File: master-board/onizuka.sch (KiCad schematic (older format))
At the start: 27 parts, among them IC1 FT232RQ, IC2 ADCMP371, P1 USB_OTG, P2 FTDI, P3 EXTRA, Q1 Q_PMOS_DGS, SW1 SWITCH_INV, U1 LD1117S33TR

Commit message: Slight schematic rework, much PCB faffing
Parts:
- removed P2: FTDI, Pin_Headers:Pin_Header_Angled_1x06, symbol CONN_01X06
- removed P3: EXTRA, Pin_Headers:Pin_Header_Angled_1x04, symbol CONN_01X04
- added P2: FTDI, Pin_Headers:Pin_Header_Angled_2x06, symbol CONN_02X06
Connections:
- no-connect marks 13 -> 14
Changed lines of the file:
@@
 L GND #PWR02
 U 1 1 573F0E0D
-P 4950 1450
-F 0 "#PWR02" H 4950 1200 50  0001 C CNN
-F 1 "GND" H 4950 1300 50  0000 C CNN
-F 2 "" H 4950 1450 50  0000 C CNN
-F 3 "" H 4950 1450 50  0000 C CNN
-	1    4950 1450
-	1    0    0    -1
-$EndComp
-Text Label 5400 1650 2    60   ~ 0
+P 4950 1900
+F 0 "#PWR02" H 4950 1650 50  0001 C CNN
+F 1 "GND" H 4950 1750 50  0000 C CNN
+F 2 "" H 4950 1900 50  0000 C CNN
+F 3 "" H 4950 1900 50  0000 C CNN
+	1    4950 1900
+	1    0    0    -1
+$EndComp
+Text Label 5400 2100 2    60   ~ 0
 PWROUT
 Wire Wire Line
@@
 	0    1    1    0
 $EndComp
-NoConn ~ 1400 2250
 $Comp
 L ADCMP371 IC2
@@
 	0    -1   -1   0
 $EndComp
-$Comp
-L CONN_01X06 P2
-U 1 1 573F91A3
-P 5600 1700
-F 0 "P2" H 5600 2050 50  0000 C CNN
-F 1 "FTDI" V 5700 1700 50  0000 C CNN
-F 2 "Pin_Headers:Pin_Header_Angled_1x06" H 5600 1700 50  0001 C CNN
-F 3 "" H 5600 1700 50  0000 C CNN
-	1    5600 1700
-	1    0    0    -1
-$EndComp
-$Comp
-L CONN_01X04 P3
-U 1 1 573F91DD
-P 5600 2300
-F 0 "P3" H 5600 2550 50  0000 C CNN
-F 1 "EXTRA" V 5700 2300 50  0000 C CNN
-F 2 "Pin_Headers:Pin_Header_Angled_1x04" H 5600 2300 50  0001 C CNN
-F 3 "" H 5600 2300 50  0000 C CNN
-	1    5600 2300
-	1    0    0    -1
-$EndComp
-Text Label 5400 1550 2    60   ~ 0
+Text Label 5400 2000 2    60   ~ 0
 CTS
-Text Label 5400 1750 2    60   ~ 0
+Text Label 5400 2200 2    60   ~ 0
 TXD
-Text Label 5400 1850 2    60   ~ 0
+Text Label 5400 2300 2    60   ~ 0
 RXD
-Text Label 5400 1950 2    60   ~ 0
+Text Label 5400 2400 2    60   ~ 0
 RTS
 Wire Wire Line
-	4950 1450 5400 1450
+	4950 1900 5400 1900
 Text Label 4400 1450 0    60   ~ 0
 TXD
@@
 Text Label 4400 2150 0    60   ~ 0
 RI
-Text Label 5400 2150 2    60   ~ 0
+Text Label 5900 1900 0    60   ~ 0
 DTR
-Text Label 5400 2250 2    60   ~ 0
+Text Label 5900 2000 0    60   ~ 0
 DSR
-Text Label 5400 2350 2    60   ~ 0
+Text Label 5900 2100 0    60   ~ 0
 DCD
-Text Label 5400 2450 2    60   ~ 0
+Text Label 5900 2200 0    60   ~ 0
 RI
+$Comp
+L CONN_02X06 P2
+U 1 1 57438536
+P 5650 2150
+F 0 "P2" H 5650 2500 50  0000 C CNN
+F 1 "FTDI" H 5650 1800 50  0000 C CNN
+F 2 "Pin_Headers:Pin_Header_Angled_2x06" H 5650 950 50  0001 C CNN
+F 3 "" H 5650 950 50  0000 C CNN
+	1    5650 2150
+	1    0    0    -1
+$EndComp
+NoConn ~ 5900 2300
+NoConn ~ 5900 2400
+$Comp
+L GND #PWR?
+U 1 1 57439366
+P 1400 2250
+F 0 "#PWR?" H 1400 2000 50  0001 C CNN
+F 1 "GND" H 1400 2100 50  0000 C CNN
+F 2 "" H 1400 2250 50  0000 C CNN
+F 3 "" H 1400 2250 50  0000 C CNN
+	1    1400 2250
+	1    0    0    -1
+$EndComp
 $EndSCHEMATC

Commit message: Various upgrades, also ESP-12E footprint for ESP board
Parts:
- added C7: 100n, Capacitors_SMD:C_0603, symbol C_Small
- added C8: 10u, Capacitors_SMD:C_0603, symbol C_Small
- added R9: 10k, Resistors_SMD:R_0603, symbol R_Small
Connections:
- net labels added: 4v5, LEDCTRL, USBD+, USBD-
- wire segments 23 -> 25
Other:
- moved on the sheet: P1

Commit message: Board reshuffle, new regulator
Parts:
- removed U1: LD1117S33TR, SOT-223, symbol LD1117S33TR
- added C9: 1u, Capacitors_SMD:C_0402, symbol C_Small
- added U1: MIC5353-3.3YMT, Housings_MLF:Thin_MLF_6_1.6mm_0.5mm_pitch, symbol MIC5353-3.3YMT
- C1, C2, C3, C4, C5, C6: footprint Capacitors_SMD:C_0603 -> Capacitors_SMD:C_0402
- C7: value 100n -> 1u; footprint Capacitors_SMD:C_0603 -> Capacitors_SMD:C_0402
- C8: value 10u -> 1u; footprint Capacitors_SMD:C_0603 -> Capacitors_SMD:C_0402
- R1, R2, R3, R4, R5, R6, R7, R8, R9: footprint Resistors_SMD:R_0603 -> Resistors_SMD:R_0402
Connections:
- wire segments 25 -> 29

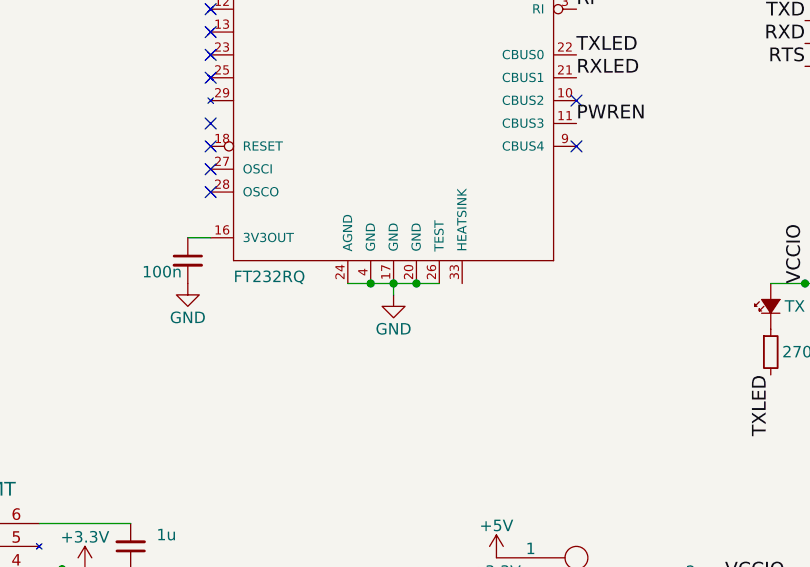
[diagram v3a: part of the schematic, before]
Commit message: Faffing, added connections to heatsink pad on FTDI, moved connector in slightly.
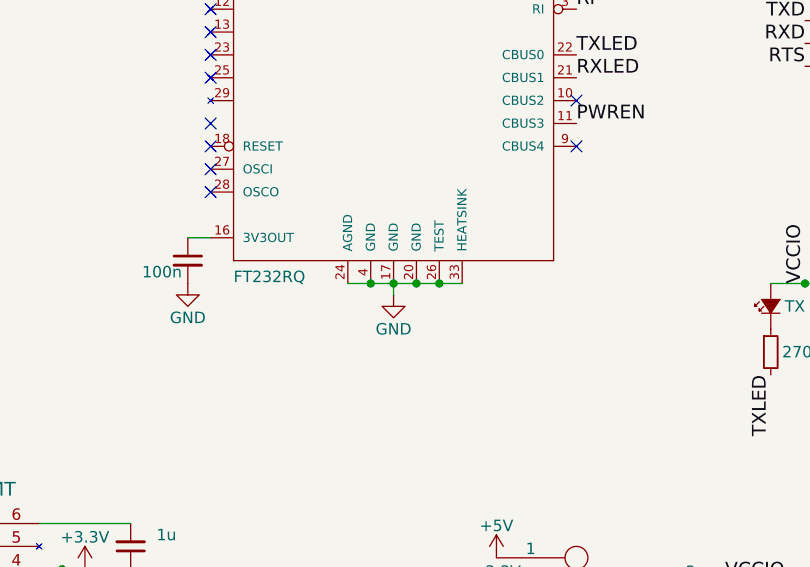
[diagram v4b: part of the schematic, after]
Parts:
- IC1: footprint Housings_DFN_QFN:QFN-32-1EP_5x5mm_Pitch0.5mm -> ftdi4-QFN-32
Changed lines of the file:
@@
 EESchema Schematic File Version 2
+LIBS:onizuka-rescue
 LIBS:power
 LIBS:device
@@
 $EndDescr
 $Comp
-L FT232RQ IC1
-U 1 1 573F0905
-P 3600 2250
-F 0 "IC1" H 2900 3170 50  0000 L BNN
-F 1 "FT232RQ" H 2900 1150 50  0000 L BNN
-F 2 "Housings_DFN_QFN:QFN-32-1EP_5x5mm_Pitch0.5mm" H 3600 2400 50  0001 C CNN
-F 3 "" H 3600 2250 60  0000 C CNN
-	1    3600 2250
-	1    0    0    -1
-$EndComp
-$Comp
 L USB_OTG P1
 U 1 1 573F0976
@@
 $EndComp
 Wire Wire Line
-	3400 3350 3800 3350
+	3400 3350 3900 3350
 Connection ~ 3600 3350
 Connection ~ 3500 3350
@@
 	1    0    0    -1
 $EndComp
+Connection ~ 3800 3350
+$Comp
+L FT232RQ IC1
+U 1 1 574DED0D
+P 3600 2250
+F 0 "IC1" H 2900 3170 50  0000 L BNN
+F 1 "FT232RQ" H 2900 1150 50  0000 L BNN
+F 2 "ftdi4-QFN-32" H 3600 2400 50  0001 C CNN
+F 3 "" H 3600 2250 60  0000 C CNN
+	1    3600 2250
+	1    0    0    -1
+$EndComp

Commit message: Tidied up schema, started to add farnell codes for components.
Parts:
- removed Q1: Q_PMOS_DGS, TO_SOT_Packages_SMD:SOT-23, symbol Q_PMOS_DGS
- added Q1: Q_PMOS_GSD, TO_SOT_Packages_SMD:SOT-23, symbol Q_PMOS_GSD
- IC1: footprint ftdi4-QFN-32 -> Housings_DFN_QFN:QFN-32-1EP_5x5mm_Pitch0.5mm
- IC2: Farnell (none) -> 2376801
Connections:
- net labels added: +4v5
- net labels removed: 4v5
- wire segments 29 -> 34
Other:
- note added: "3v3 Regulator"
- note added: "FTDI"
- note added: "Output Voltage Control"
- note added: "Output power control"
- note added: "Output voltage sense"
- note added: "USB Connector"
- note added: "Voltage Ref"
- moved on the sheet: IC1, P2, U1

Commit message: Various tweaks
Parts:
- removed C2: 10n, Capacitors_SMD:C_0402, symbol CP_Small
- removed C3: 4.7u, Capacitors_SMD:C_0402, symbol CP_Small
- added C2: 10n, Capacitors_SMD:C_0402, symbol C_Small
- added C3: 4u7, Capacitors_SMD:C_0402, symbol C_Small
- IC1: footprint Housings_DFN_QFN:QFN-32-1EP_5x5mm_Pitch0.5mm -> ftdi:FTDI-FT232RQ-QFN-32
- R1, R2, R3: value 270R -> 1k
- R4: value 1k -> 1K
- R5: value 510K -> 51K
- R6: value 4M3 -> 430K
- R7, R8: value 680R -> 1k
- R9: value 10k -> 10K
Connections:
- net +5V: now also C2.1, C3.1
- net GND: now also C2.2, C3.2
- net +4v5: no longer names the net of IC2.3 (-), R5.2, R6.1
- no-connect marks 14 -> 8
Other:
- note removed: "Output voltage sense"
- note removed: "Voltage Ref"

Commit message: Updated switch
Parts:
- removed SW1: SWITCH_INV, Buttons_Switches_ThroughHole:SW_Micro_SPST, symbol SWITCH_INV
- added SW1: SPDT, Wurth:450301014042, symbol SPDT
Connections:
- net +3V3: now also SW1.3
- net +5V: now also SW1.2
- net VCCIO: now also SW1.1
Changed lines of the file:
@@
 LIBS:contrib
 LIBS:valves
-LIBS:ftdi
 LIBS:ad
 LIBS:micrel
-LIBS:power-ext
+LIBS:ftdi
+LIBS:Switches
 LIBS:onizuka-cache
 EELAYER 25 0
@@
 $EndComp
 $Comp
-L SWITCH_INV SW1
-U 1 1 573F1E28
-P 5500 2850
-F 0 "SW1" H 5300 3000 50  0001 C CNN
-F 1 "SWITCH_INV" H 5350 2700 50  0001 C CNN
-F 2 "Buttons_Switches_ThroughHole:SW_Micro_SPST" H 5500 2850 50  0001 C CNN
-F 3 "" H 5500 2850 50  0000 C CNN
-	1    5500 2850
-	-1   0    0    -1
-$EndComp
-$Comp
 L +5V #PWR010
 U 1 1 573F1E7D
-P 5000 2750
-F 0 "#PWR010" H 5000 2600 50  0001 C CNN
-F 1 "+5V" H 5000 2890 50  0000 C CNN
-F 2 "" H 5000 2750 50  0000 C CNN
-F 3 "" H 5000 2750 50  0000 C CNN
-	1    5000 2750
+P 5150 2750
+F 0 "#PWR010" H 5150 2600 50  0001 C CNN
+F 1 "+5V" H 5150 2890 50  0000 C CNN
+F 2 "" H 5150 2750 50  0000 C CNN
+F 3 "" H 5150 2750 50  0000 C CNN
+	1    5150 2750
 	-1   0    0    -1
 $EndComp
@@
 L +3.3V #PWR011
 U 1 1 573F1E91
-P 5000 2950
-F 0 "#PWR011" H 5000 2800 50  0001 C CNN
-F 1 "+3.3V" H 5000 3090 50  0000 C CNN
-F 2 "" H 5000 2950 50  0000 C CNN
-F 3 "" H 5000 2950 50  0000 C CNN
-	1    5000 2950
+P 5150 2950
+F 0 "#PWR011" H 5150 2800 50  0001 C CNN
+F 1 "+3.3V" H 5150 3090 50  0000 C CNN
+F 2 "" H 5150 2950 50  0000 C CNN
+F 3 "" H 5150 2950 50  0000 C CNN
+	1    5150 2950
 	-1   0    0    -1
 $EndComp
-Text Label 6000 2850 0    60   ~ 0
+Text Label 5950 2850 0    60   ~ 0
 VCCIO
 Text Label 2900 3250 2    60   ~ 0
@@
 L PWR_FLAG #FLG013
 U 1 1 573F27A3
-P 6000 2850
-F 0 "#FLG013" H 6000 2945 50  0001 C CNN
-F 1 "PWR_FLAG" H 6000 3030 50  0000 C CNN
-F 2 "" H 6000 2850 50  0000 C CNN
-F 3 "" H 6000 2850 50  0000 C CNN
-	1    6000 2850
+P 5950 2850
+F 0 "#FLG013" H 5950 2945 50  0001 C CNN
+F 1 "PWR_FLAG" H 5950 3030 50  0000 C CNN
+F 2 "" H 5950 2850 50  0000 C CNN
+F 3 "" H 5950 2850 50  0000 C CNN
+	1    5950 2850
 	-1   0    0    1
 $EndComp
@@
 	1    0    0    -1
 $EndComp
-Connection ~ 6000 2850
+Connection ~ 5950 2850
 $Comp
 L FT232RQ IC1
@@
 	1    0    0    -1
 $EndComp
+$Comp
+L SPDT SW1
+U 1 1 574EF3CB
+P 5550 2850
+F 0 "SW1" H 5550 2500 60  0001 C CNN
+F 1 "SPDT" H 5550 3150 60  0001 C CNN
+F 2 "Wurth:450301014042" H 5600 2850 60  0001 C CNN
+F 3 "" H 5600 2850 60  0000 C CNN
+	1    5550 2850
+	1    0    0    -1
+$EndComp

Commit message: Poked around, fixed minor bug, tweaked silk slightly.
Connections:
- net +5V: no longer R9.1
- net VCCIO: now also R9.1
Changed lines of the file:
@@
 	2900 3900 2900 3800
 Connection ~ 3100 3900
-$Comp
-L +5V #PWR018
-U 1 1 5744B5FA
-P 2900 3600
-F 0 "#PWR018" H 2900 3450 50  0001 C CNN
-F 1 "+5V" H 2900 3740 50  0000 C CNN
-F 2 "" H 2900 3600 50  0000 C CNN
-F 3 "" H 2900 3600 50  0000 C CNN
-	1    2900 3600
-	-1   0    0    -1
-$EndComp
 Text Label 5950 3750 0    60   ~ 0
 LEDCTRL
@@
 	1    0    0    -1
 $EndComp
+Text Label 2900 3600 2    60   ~ 0
+VCCIO
 $EndSCHEMATC
